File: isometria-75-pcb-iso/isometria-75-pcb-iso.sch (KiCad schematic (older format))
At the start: 26 parts, among them J101 USB, J102 SPI, J103 Conn_01x06_Male, Q101 AO3400A, SW101 RST, SW102 BOOT, U101 XC6206P332MR, U102 STM32F072CBTx

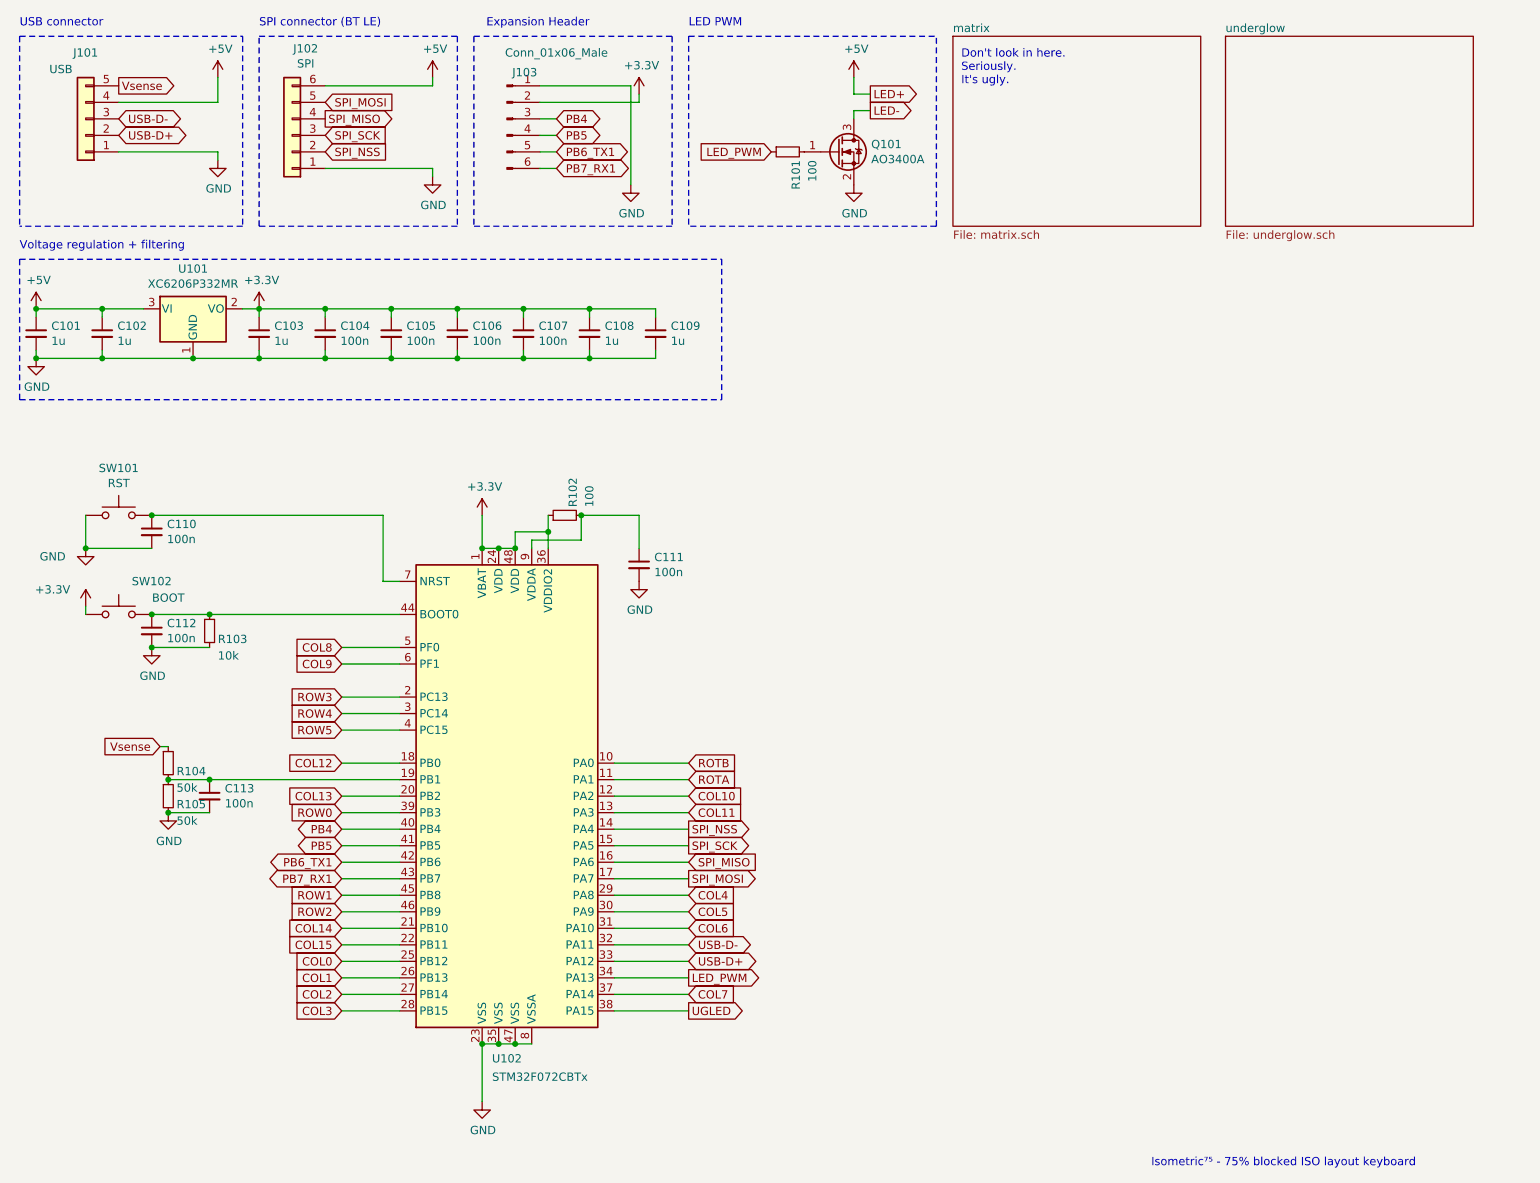
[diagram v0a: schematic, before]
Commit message: renamed pcb file, added 3d models
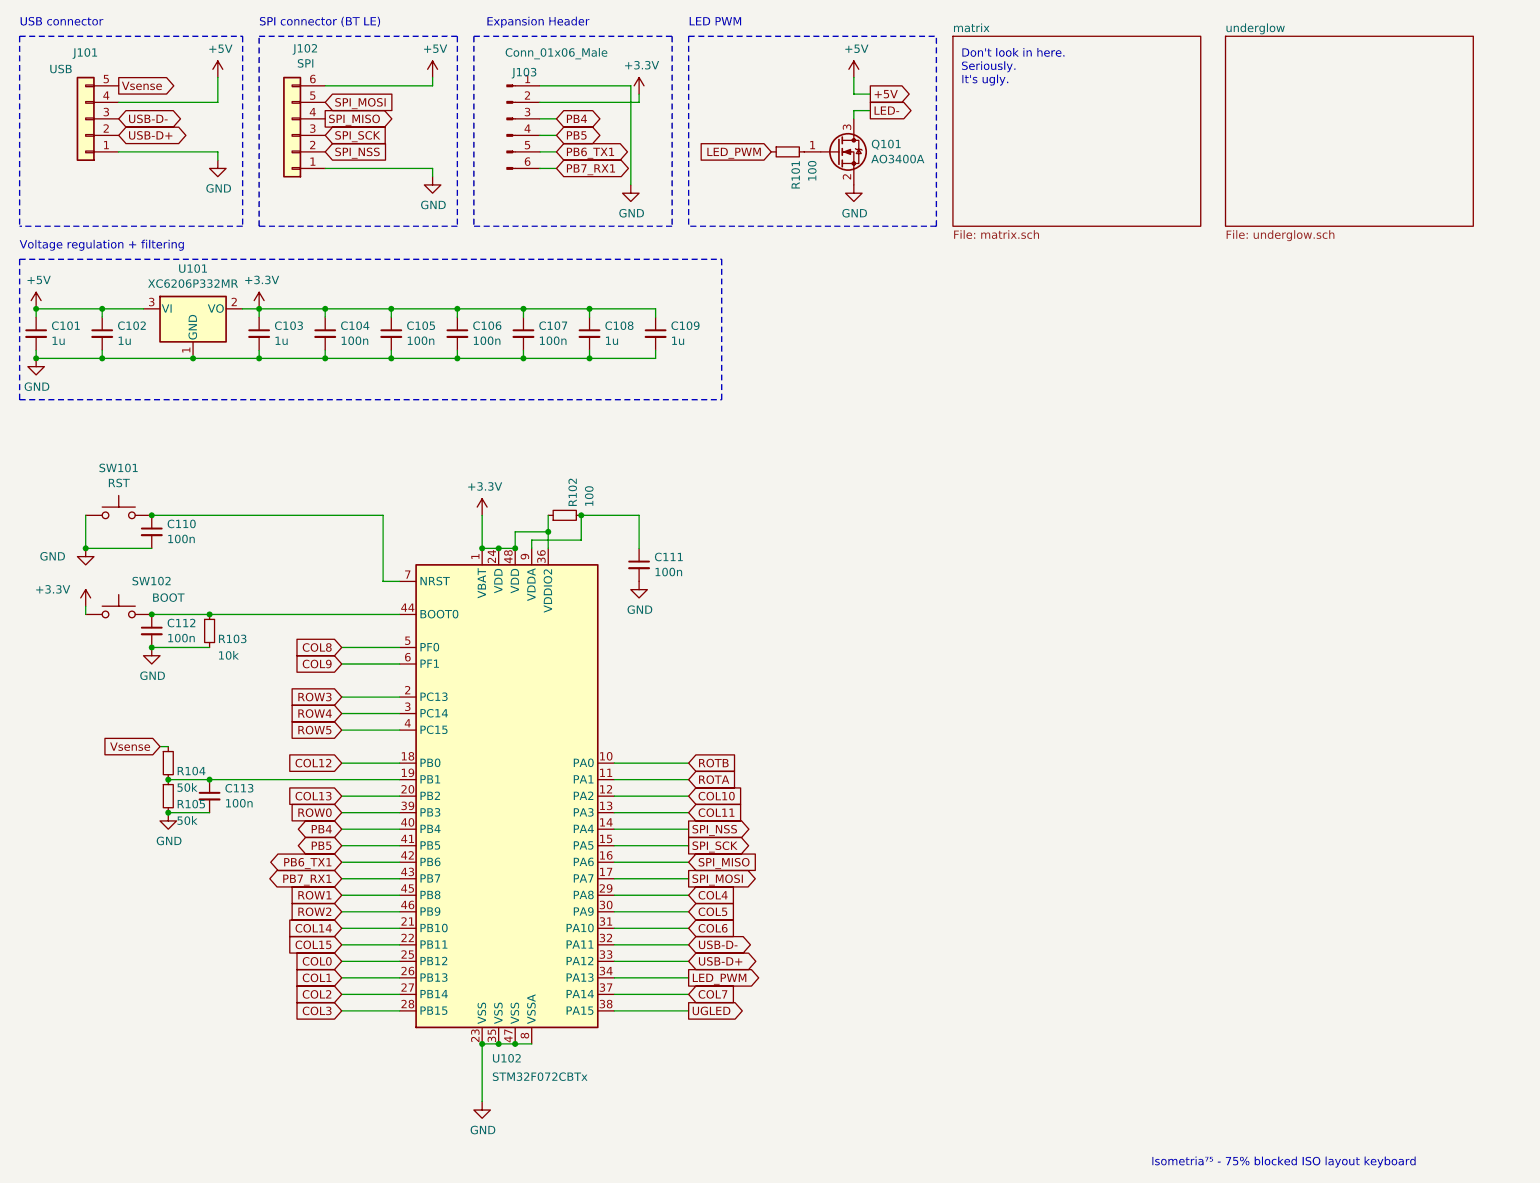
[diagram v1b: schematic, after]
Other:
- note added: "Isometria⁷⁵ - 75% blocked ISO layout keyboard"
- note removed: "Isometric⁷⁵ - 75% blocked ISO layout keyboard"
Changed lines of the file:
@@
 $EndComp
 Text GLabel 5700 1000 2    50   Output ~ 0
-LED+
++5V
 Text GLabel 5700 1100 2    50   Output ~ 0
 LED-
@@
 Don't look in here.\nSeriously. \nIt's ugly.\n
 Text Notes 7400 7500 0    50   ~ 0
-Isometric⁷⁵ - 75% blocked ISO layout keyboard
+Isometria⁷⁵ - 75% blocked ISO layout keyboard
 Text GLabel 4600 6450 2    50   Input ~ 0
 COL7

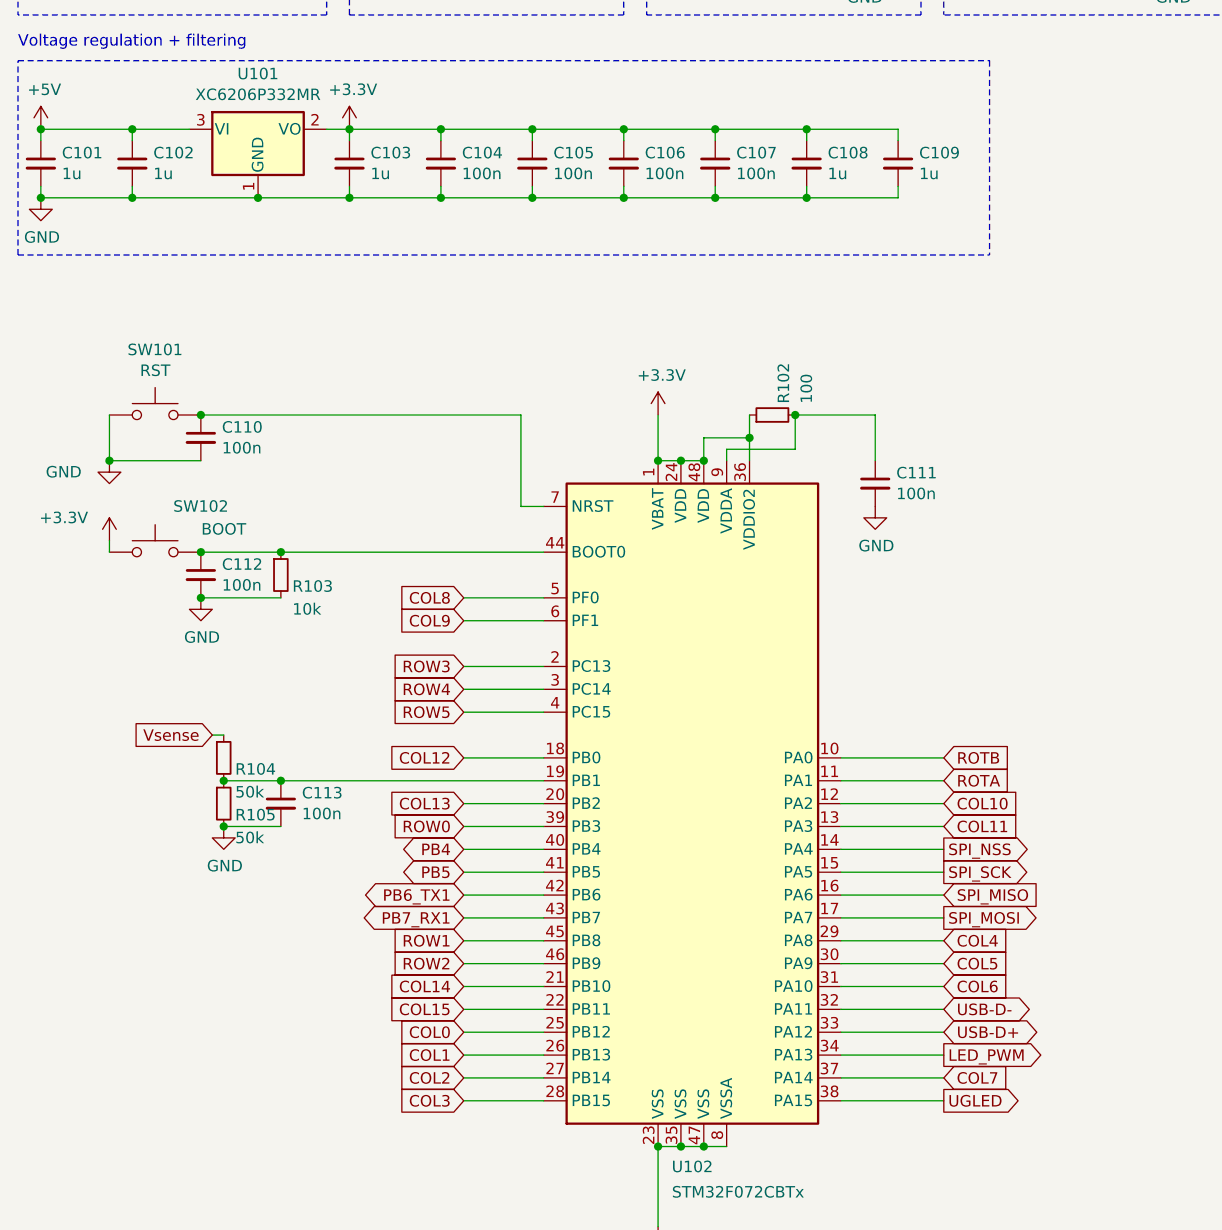
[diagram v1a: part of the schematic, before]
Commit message: changed led backlight to a different pin
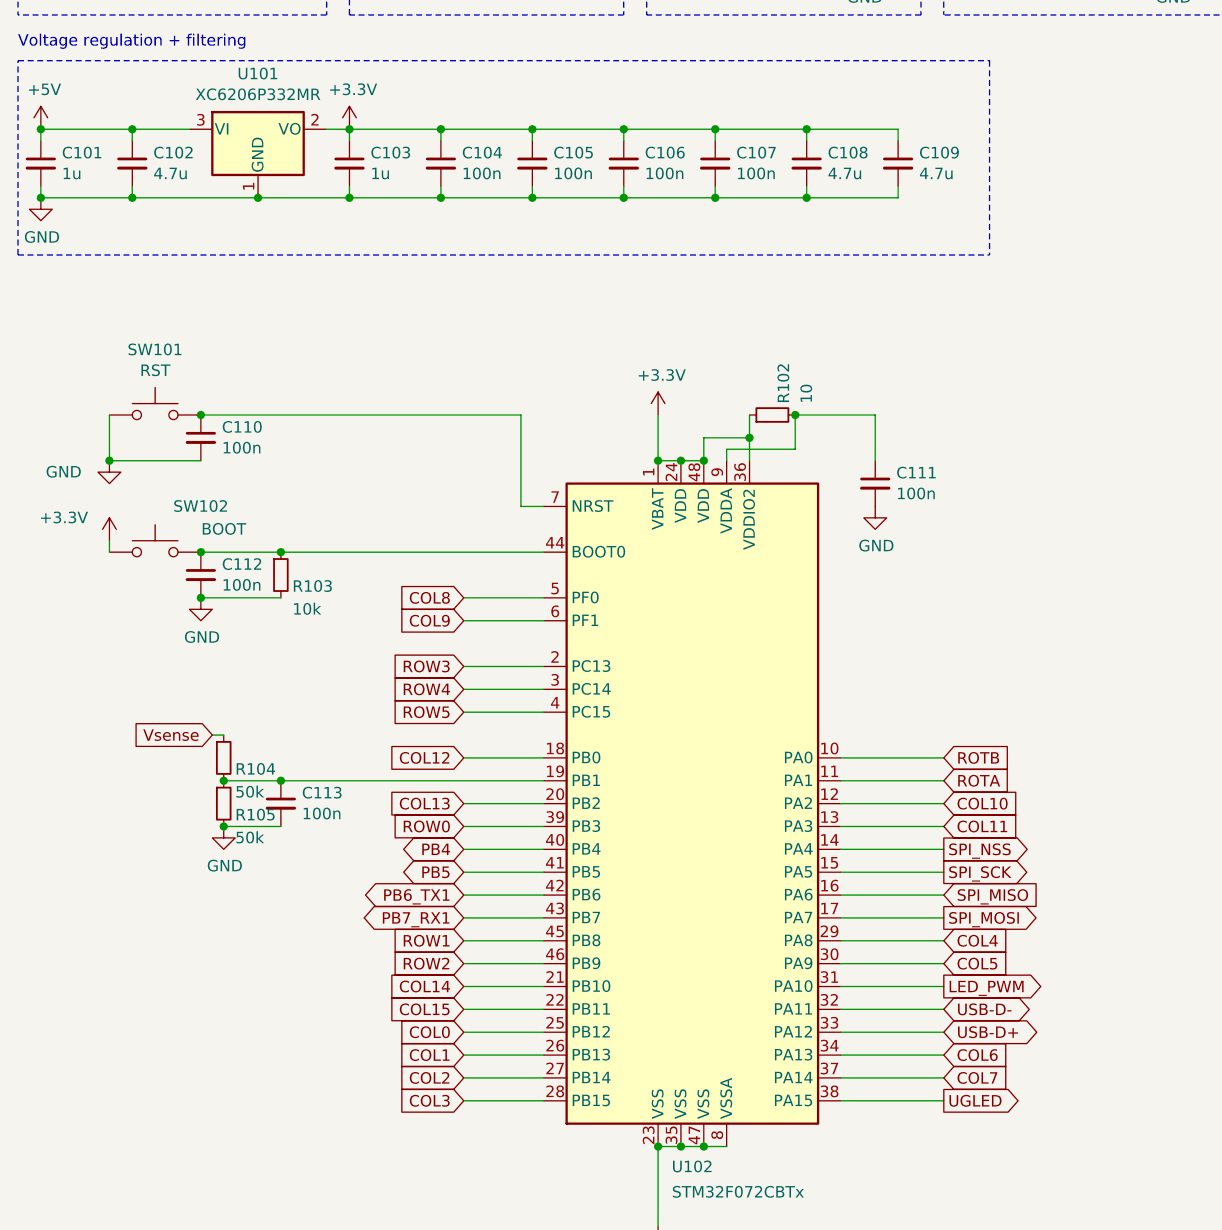
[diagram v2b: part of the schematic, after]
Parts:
- C102, C108, C109: value 1u -> 4.7u
- R102: value 100 -> 10
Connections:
- net COL6: now also U102.34 (PA13); no longer U102.31 (PA10)
- net LED_PWM: now also U102.31 (PA10); no longer U102.34 (PA13)
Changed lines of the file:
@@
 P 3850 3550
 F 0 "R102" H 3900 3500 50  0000 L CNN
-F 1 "100" H 3900 3400 50  0000 L CNN
+F 1 "10" H 3900 3400 50  0000 L CNN
 F 2 "Resistor_SMD:R_0402_1005Metric" H 3850 3550 50  0001 C CNN
 F 3 "~" H 3850 3550 50  0001 C CNN
@@
 Text GLabel 5100 1350 0    50   Input ~ 0
 LED_PWM
-Text GLabel 4600 6350 2    50   Output ~ 0
+Text GLabel 4600 6050 2    50   Output ~ 0
 LED_PWM
 Wire Wire Line
@@
 P 4000 2450
 F 0 "C108" H 4092 2496 50  0000 L CNN
-F 1 "1u" H 4092 2405 50  0000 L CNN
+F 1 "4.7u" H 4092 2405 50  0000 L CNN
 F 2 "Capacitor_SMD:C_0402_1005Metric" H 4000 2450 50  0001 C CNN
 F 3 "~" H 4000 2450 50  0001 C CNN
@@
 P 1050 2450
 F 0 "C102" H 1142 2496 50  0000 L CNN
-F 1 "1u" H 1142 2405 50  0000 L CNN
+F 1 "4.7u" H 1142 2405 50  0000 L CNN
 F 2 "Capacitor_SMD:C_0603_1608Metric" H 1050 2450 50  0001 C CNN
 F 3 "~" H 1050 2450 50  0001 C CNN
@@
 P 4400 2450
 F 0 "C109" H 4492 2496 50  0000 L CNN
-F 1 "1u" H 4492 2405 50  0000 L CNN
+F 1 "4.7u" H 4492 2405 50  0000 L CNN
 F 2 "Capacitor_SMD:C_0603_1608Metric" H 4400 2450 50  0001 C CNN
 F 3 "~" H 4400 2450 50  0001 C CNN
@@
 Text GLabel 4600 5950 2    50   Input ~ 0
 COL5
-Text GLabel 4600 6050 2    50   Input ~ 0
+Text GLabel 4600 6350 2    50   Input ~ 0
 COL6
 Wire Wire Line

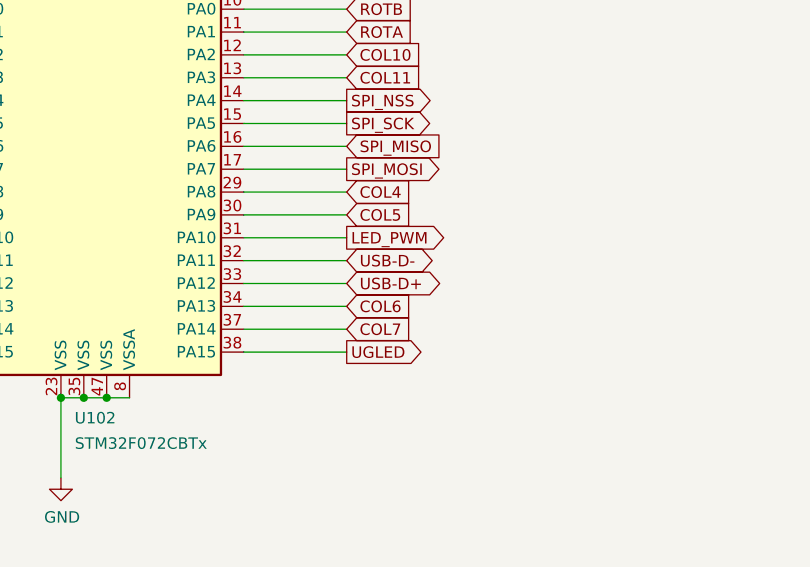
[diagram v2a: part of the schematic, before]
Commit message: moved UGLED to a HW PWM pin, improved some trace routing
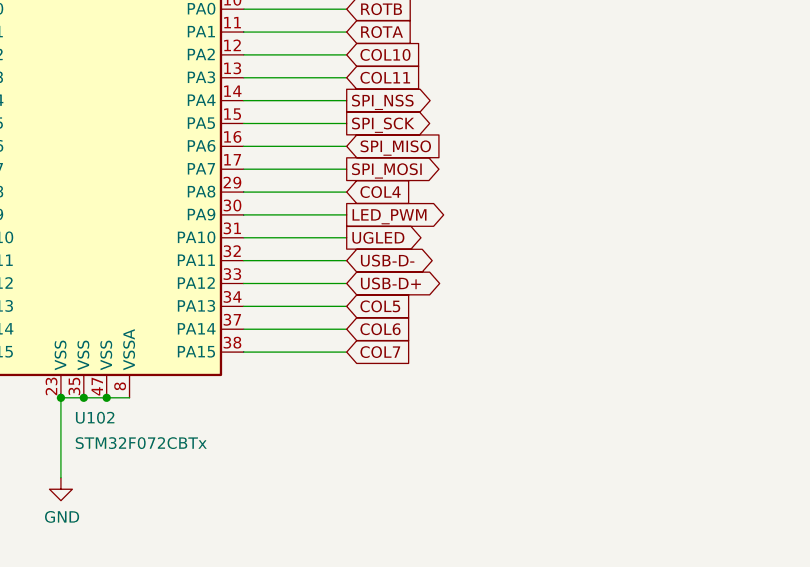
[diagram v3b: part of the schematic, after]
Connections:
- net COL5: now also U102.34 (PA13); no longer U102.30 (PA9)
- net COL6: now also U102.37 (PA14); no longer U102.34 (PA13)
- net COL7: now also U102.38 (PA15); no longer U102.37 (PA14)
- net LED_PWM: now also U102.30 (PA9); no longer U102.31 (PA10)
- net UGLED: now also U102.31 (PA10); no longer U102.38 (PA15)
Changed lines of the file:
@@
 Text GLabel 5100 1350 0    50   Input ~ 0
 LED_PWM
-Text GLabel 4600 6050 2    50   Output ~ 0
+Text GLabel 4600 5950 2    50   Output ~ 0
 LED_PWM
 Wire Wire Line
@@
 Text GLabel 4600 5850 2    50   Input ~ 0
 COL4
-Text GLabel 4600 5950 2    50   Input ~ 0
+Text GLabel 4600 6350 2    50   Input ~ 0
 COL5
-Text GLabel 4600 6350 2    50   Input ~ 0
+Text GLabel 4600 6450 2    50   Input ~ 0
 COL6
 Wire Wire Line
@@
 Text Notes 7400 7500 0    50   ~ 0
 Isometria⁷⁵ - 75% blocked ISO layout keyboard
-Text GLabel 4600 6450 2    50   Input ~ 0
+Text GLabel 4600 6550 2    50   Input ~ 0
 COL7
 Wire Wire Line
@@
 F1 "underglow.sch" 50
 $EndSheet
-Text GLabel 4600 6550 2    50   Output ~ 0
+Text GLabel 4600 6050 2    50   Output ~ 0
 UGLED
 Wire Wire Line

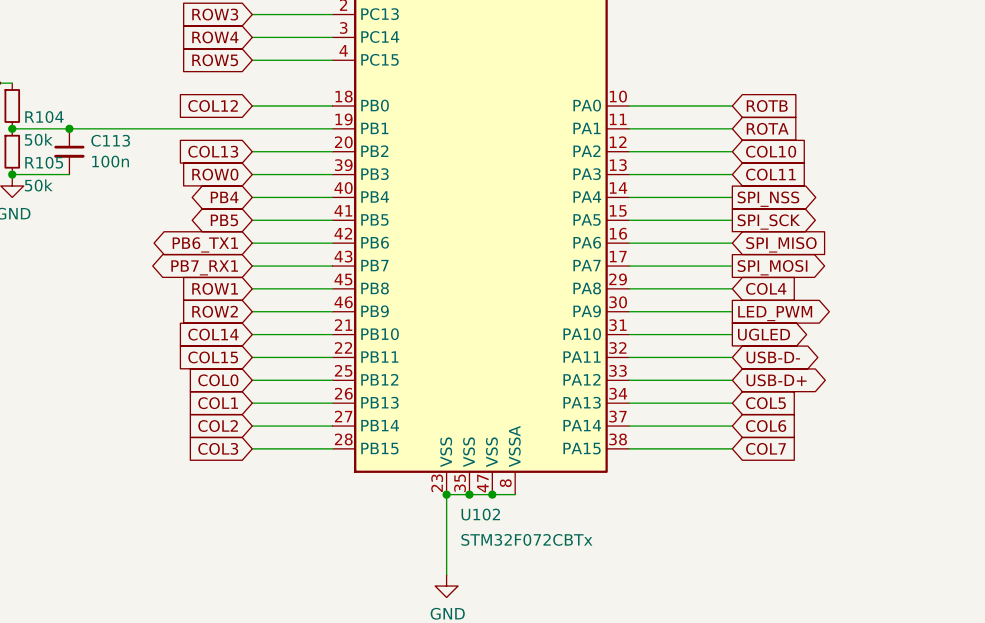
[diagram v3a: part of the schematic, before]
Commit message: moved underglow from TIM1 to TIM2
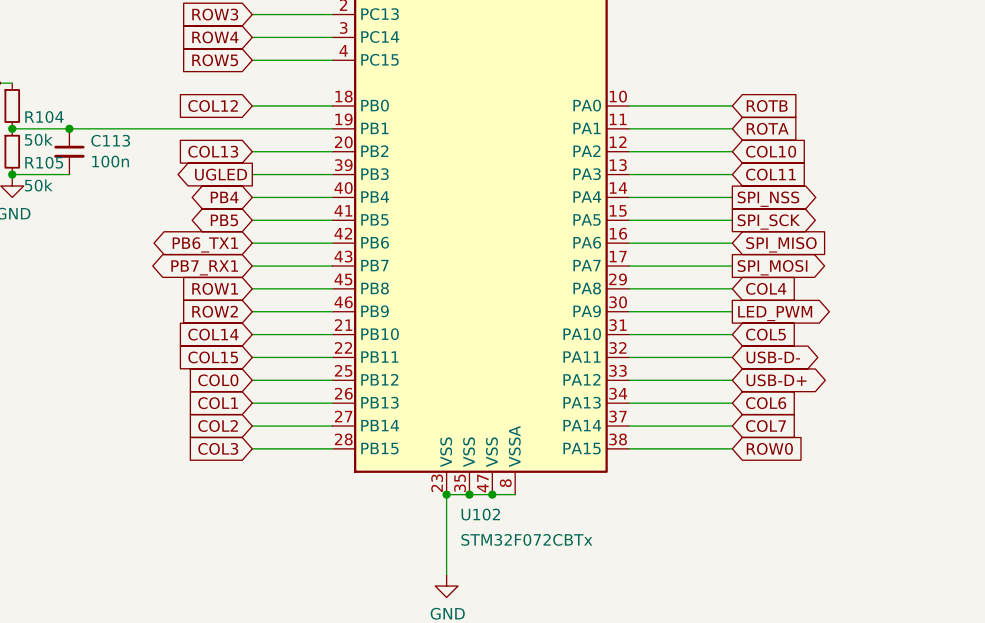
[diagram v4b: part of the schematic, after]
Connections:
- net COL5: now also U102.31 (PA10); no longer U102.34 (PA13)
- net COL6: now also U102.34 (PA13); no longer U102.37 (PA14)
- net COL7: now also U102.37 (PA14); no longer U102.38 (PA15)
- net ROW0: now also U102.38 (PA15); no longer U102.39 (PB3)
- net UGLED: now also U102.39 (PB3); no longer U102.31 (PA10)
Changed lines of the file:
@@
 Text GLabel 4600 5850 2    50   Input ~ 0
 COL4
+Text GLabel 4600 6050 2    50   Input ~ 0
+COL5
 Text GLabel 4600 6350 2    50   Input ~ 0
-COL5
-Text GLabel 4600 6450 2    50   Input ~ 0
 COL6
 Wire Wire Line
@@
 Text Notes 7400 7500 0    50   ~ 0
 Isometria⁷⁵ - 75% blocked ISO layout keyboard
-Text GLabel 4600 6550 2    50   Input ~ 0
+Text GLabel 4600 6450 2    50   Input ~ 0
 COL7
 Wire Wire Line
@@
 Text GLabel 2500 5850 0    50   Input ~ 0
 ROW1
-Text GLabel 2500 5350 0    50   Input ~ 0
+Text GLabel 4600 6550 2    50   Input ~ 0
 ROW0
 Wire Wire Line
@@
 F1 "underglow.sch" 50
 $EndSheet
-Text GLabel 4600 6050 2    50   Output ~ 0
+Text GLabel 2500 5350 0    50   Output ~ 0
 UGLED
 Wire Wire Line
